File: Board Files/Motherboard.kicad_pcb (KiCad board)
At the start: 2 copper layers, 106.1 x 155 mm, 77 parts, among them P1 72-Pin Connector, P2 PowerSw, P3 ResetSw, P4 Controller_Port, P6 RF-Mod, Q1 2SA937, Q2 2SC2021, T1 08RB01, U1 6116 (WRAM), U2 74HC373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

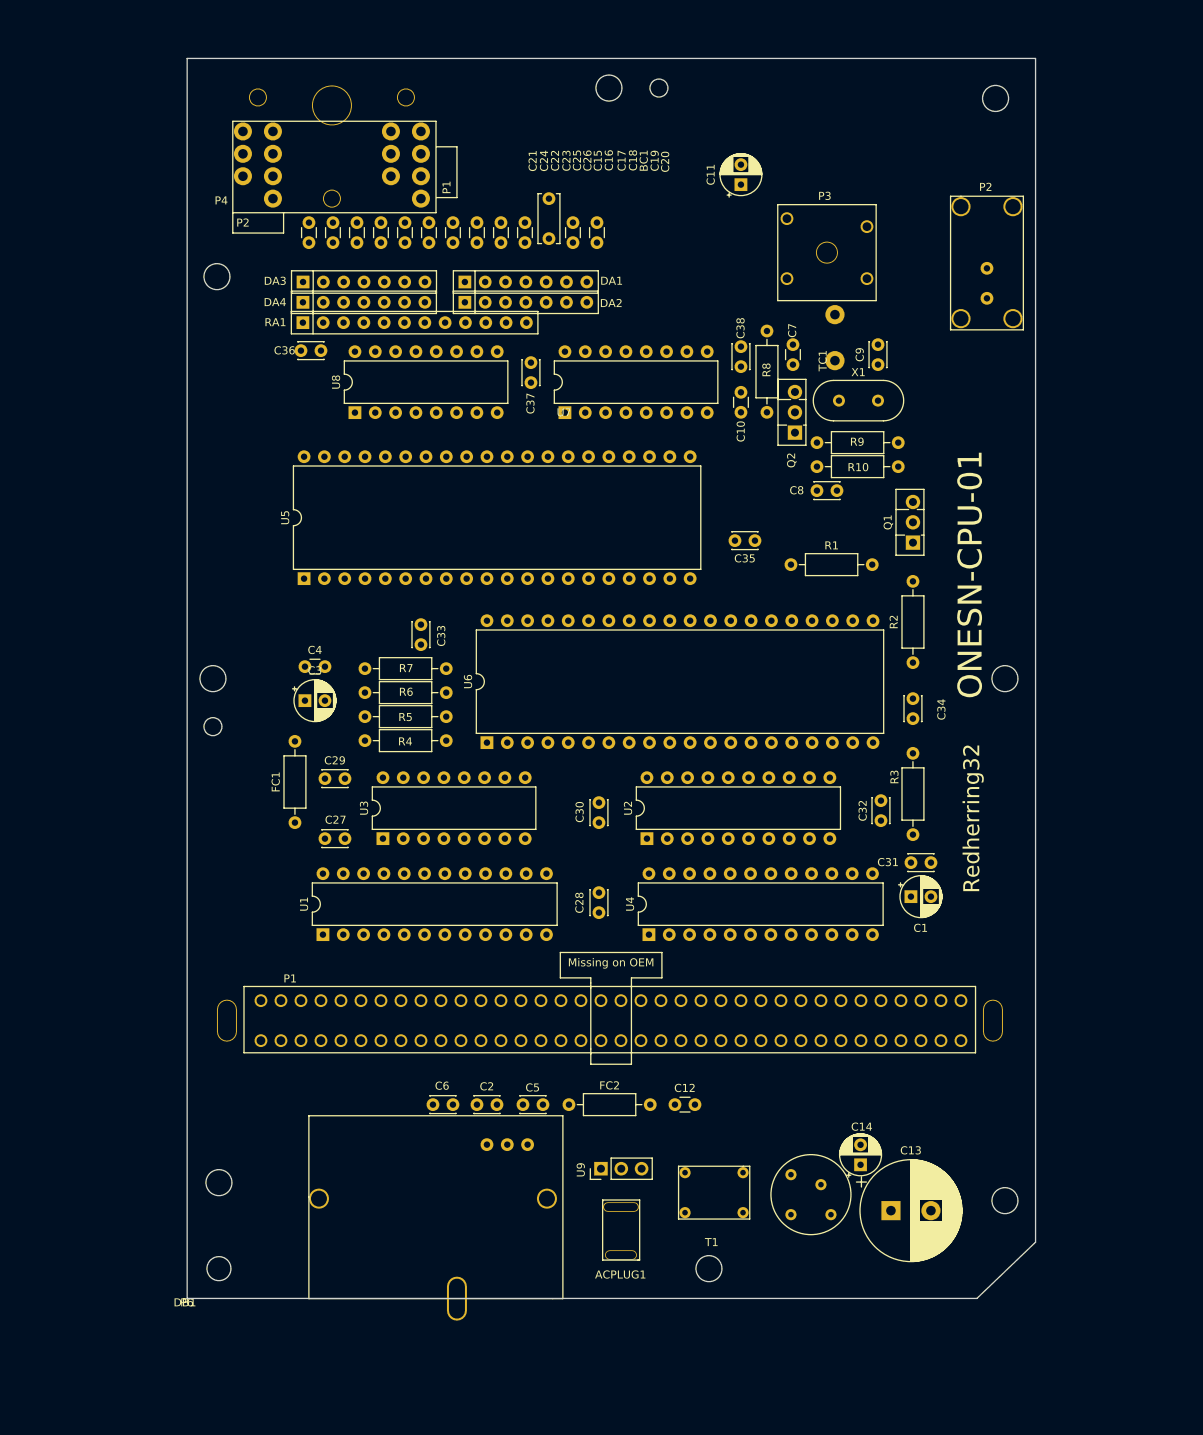
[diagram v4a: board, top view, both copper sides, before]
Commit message: Almost done
+ Added zone cutouts to make copper pours more like OEM shape
+ Edited schematic to be more readable

TO-DO:
* Finish cutouts
* Verify mounting, alignment, and connector hole placement and sizing.
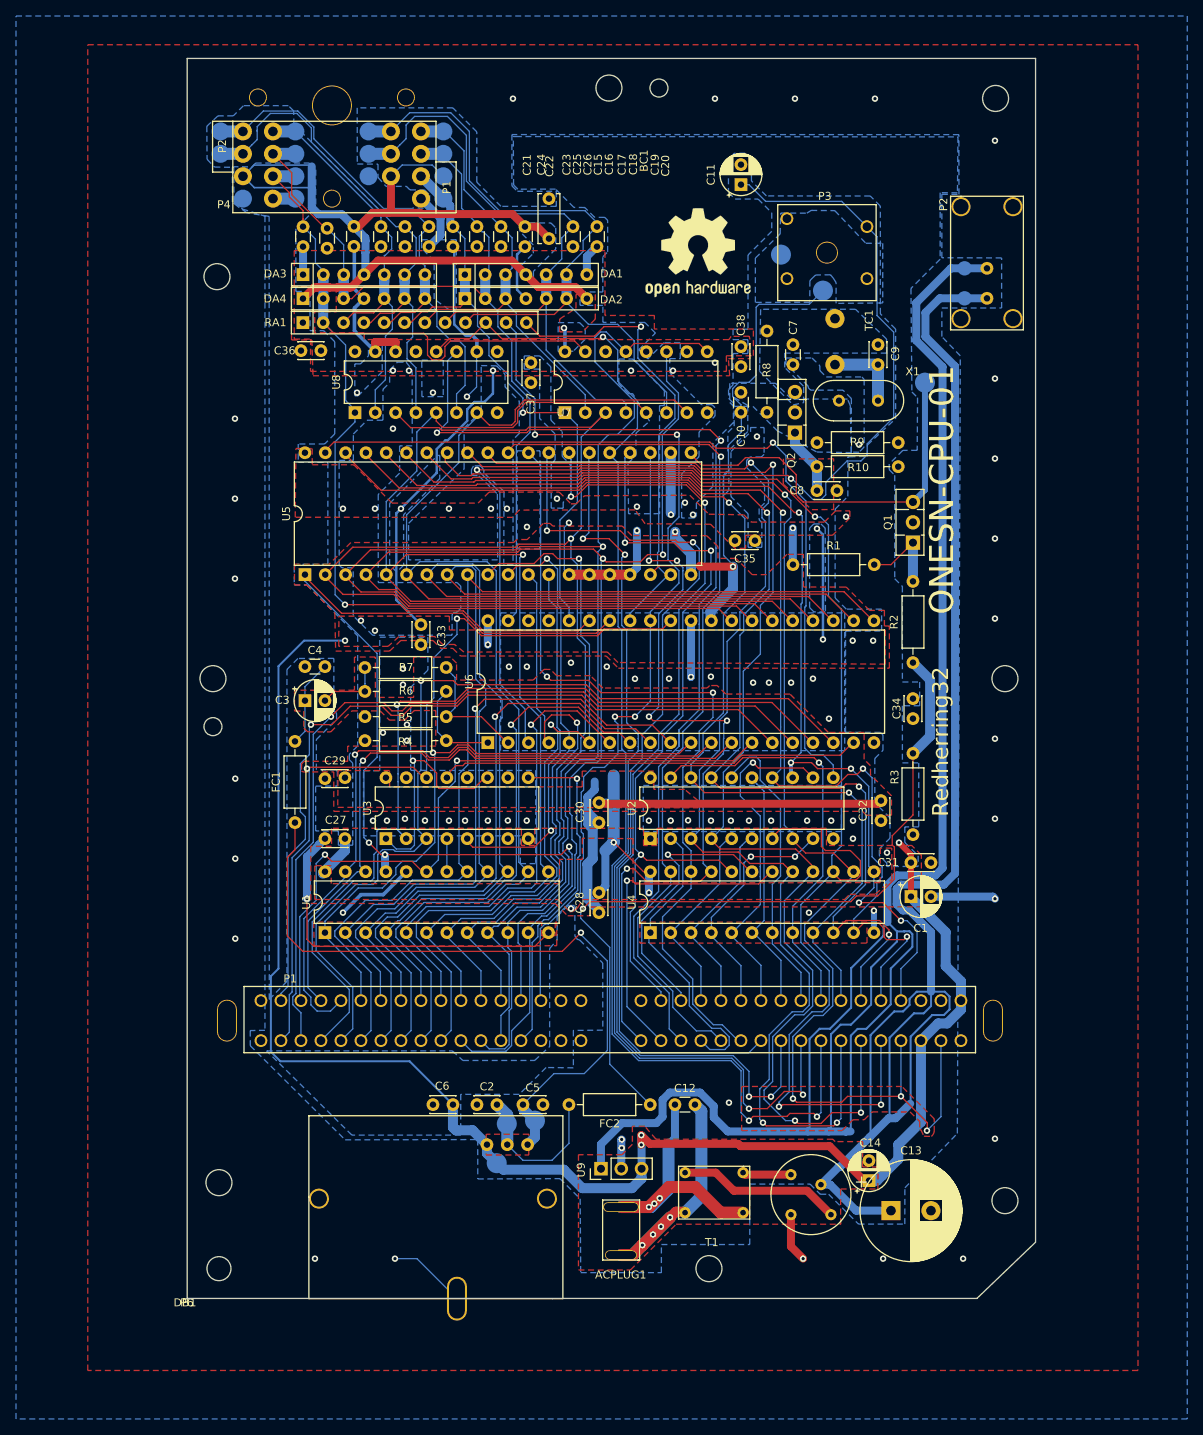
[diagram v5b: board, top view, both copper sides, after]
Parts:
- added  : TestPoint_Pad_D2.5mm, TestPoint:TestPoint_Pad_D2.5mm, B.Cu at (38.7, -16.9)
- added  : TestPoint_Pad_D2.5mm, TestPoint:TestPoint_Pad_D2.5mm, B.Cu at (40.0, -21.9)
- added  : TestPoint_Pad_D2.5mm, TestPoint:TestPoint_Pad_D2.5mm, B.Cu at (43.6, -21.9)
- added  : TestPoint_Pad_D2.5mm, TestPoint:TestPoint_Pad_D2.5mm, B.Cu at (92.2, -114.5)
- added  : TestPoint_Pad_D2.5mm, TestPoint:TestPoint_Pad_D2.5mm, B.Cu at (74.2, -130.5)
- added  : TestPoint_Pad_D2.5mm, TestPoint:TestPoint_Pad_D2.5mm, B.Cu at (79.5, -126.0)
- added REF**: OSHW-Logo2_14.6x12mm_SilkScreen, Symbol:OSHW-Logo2_14.6x12mm_SilkScreen, F.Cu at (63.9, -130.8)
- moved FC2 10.2 mm to (57.9, -24.2), turned to 180 degrees
- moved C14 2.24 mm to (85.2, -14.8)
- moved C22 1.01 mm to (17.5, -133.8)
- moved DA1 0.92 mm to (34.7, -128.0)
- moved DA3 0.92 mm to (14.5, -128.0)
- moved C21 0.89 mm to (14.5, -134.0)
- moved C24 0.60 mm to (20.9, -131.5)
- moved U5 0.51 mm to (14.8, -90.5)
- moved C15 0.50 mm to (33.2, -134.0)
- moved C16 0.50 mm to (36.2, -134.0)
- moved C17 0.50 mm to (39.2, -134.0)
- moved C18 0.50 mm to (42.2, -134.0)
- moved C19 0.50 mm to (48.2, -134.0)
- moved C20 0.50 mm to (51.2, -134.0)
- moved C23 0.50 mm to (24.2, -134.0)
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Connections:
- net /CIC-TO-CART renamed Net-(P1-Pad34)
- net /CIC-TO-MB renamed Net-(P1-Pad35)
- C11 pad 1: /RST -> /~RST
- C12 pad 1: Net-(C12-Pad1) -> Net-(ACPLUG1-Pad2)
- C12 pad 2: Net-(C12-Pad2) -> Net-(ACPLUG1-Pad1)
- C24 pad 2: Net-(C24-Pad2) -> /VCC
- C7 pad 1: Net-(C7-Pad1) -> /GND
- C7 pad 2: /GND -> Net-(C7-Pad2)
- C9 pad 2: Net-(C7-Pad1) -> Net-(C7-Pad2)
- DB1 pad 3: Net-(C12-Pad1) -> Net-(DB1-Pad3)
- DB1 pad 4: Net-(C12-Pad2) -> Net-(DB1-Pad4)
- FC2 pad 1: /VIDEO -> Net-(FC2-Pad1)
- FC2 pad 2: Net-(FC2-Pad2) -> /VIDEO
- P1 pad 70: /CIC-RST -> /VCC
- P3 pad 1: /RST -> /~RST
- P4 pad 3: (no net) -> /GND
- P4 pad 4: (no net) -> /GND
- P4 pad 5: (no net) -> /GND
- P4 pad 6: (no net) -> /GND
- Q2 pad 3: Net-(C7-Pad1) -> Net-(C7-Pad2)
- R2 pad 1: Net-(FC2-Pad2) -> Net-(FC2-Pad1)
- R3 pad 2: Net-(FC2-Pad2) -> Net-(FC2-Pad1)
- R6 pad 1: /SOUND-1 -> Net-(C3-Pad2)
- R6 pad 2: Net-(C3-Pad2) -> /SOUND-1
- R7 pad 1: /SOUND-2 -> Net-(C3-Pad2)
- R7 pad 2: Net-(C3-Pad2) -> /SOUND-2
- R8 pad 2: Net-(C7-Pad1) -> Net-(C7-Pad2)
- R9 pad 1: /VCC -> Net-(C10-Pad2)
- R9 pad 2: Net-(C10-Pad2) -> /VCC
- T1 pad 2: Net-(C12-Pad1) -> Net-(DB1-Pad4)
- T1 pad 4: Net-(C12-Pad2) -> Net-(DB1-Pad3)
- TC1 pad 1: Net-(C7-Pad1) -> Net-(C9-Pad1)
- TC1 pad 2: Net-(C9-Pad1) -> Net-(C7-Pad2)
- U7 pad 11: /CPU-D4 -> /CPU-D2
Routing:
- net /VCC: track 0.00 -> 465.4 mm, vias 0 -> 36
- net Net-(P2-Pad2): track 0.00 -> 228.9 mm
- net /GND: track 0.00 -> 215.8 mm, vias 0 -> 78
- net /CPU-D1: track 0.00 -> 209.3 mm, vias 0 -> 1
- net /CPU-D0: track 0.00 -> 204.6 mm, vias 0 -> 1
- net /CPU-D3: track 0.00 -> 202.6 mm, vias 0 -> 1
- net /CPU-D4: track 0.00 -> 194.6 mm
- net /CPU-D2: track 0.00 -> 194.5 mm, vias 0 -> 2
- net Net-(C13-Pad1): track 0.00 -> 189.6 mm
- net /PPU-D4: track 0.00 -> 174.7 mm, vias 0 -> 4
- net /PPU-D5: track 0.00 -> 174.5 mm, vias 0 -> 3
- net /PPU-D6: track 0.00 -> 162.0 mm, vias 0 -> 3
- net /PPU-A13: track 0.00 -> 159.3 mm, vias 0 -> 3
- net /PPU-D7: track 0.00 -> 157.7 mm, vias 0 -> 3
- net /PPU-D1: track 0.00 -> 149.1 mm, vias 0 -> 3
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- added copper zone on B.Cu, net /GND
- added copper zone on F.Cu, net /GND
- added copper zone on B.Cu, net /SYS-CLK
- added copper zone on B.Cu, net /VCC
- added copper zone on F.Cu, net /VCC
- added copper zone on B.Cu, net Net-(C10-Pad2)
- added copper zone on B.Cu, net Net-(C7-Pad2)
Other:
- net class Default: trace_width 0.25 -> 0.155
- net class Thin added: clearance 0.15, trace_width 0.15, via_dia 0.8, via_drill 0.4
- rule solder_mask_min_width: 0.25 -> 0.155
- rule trace_min: 0.2 -> 0.127

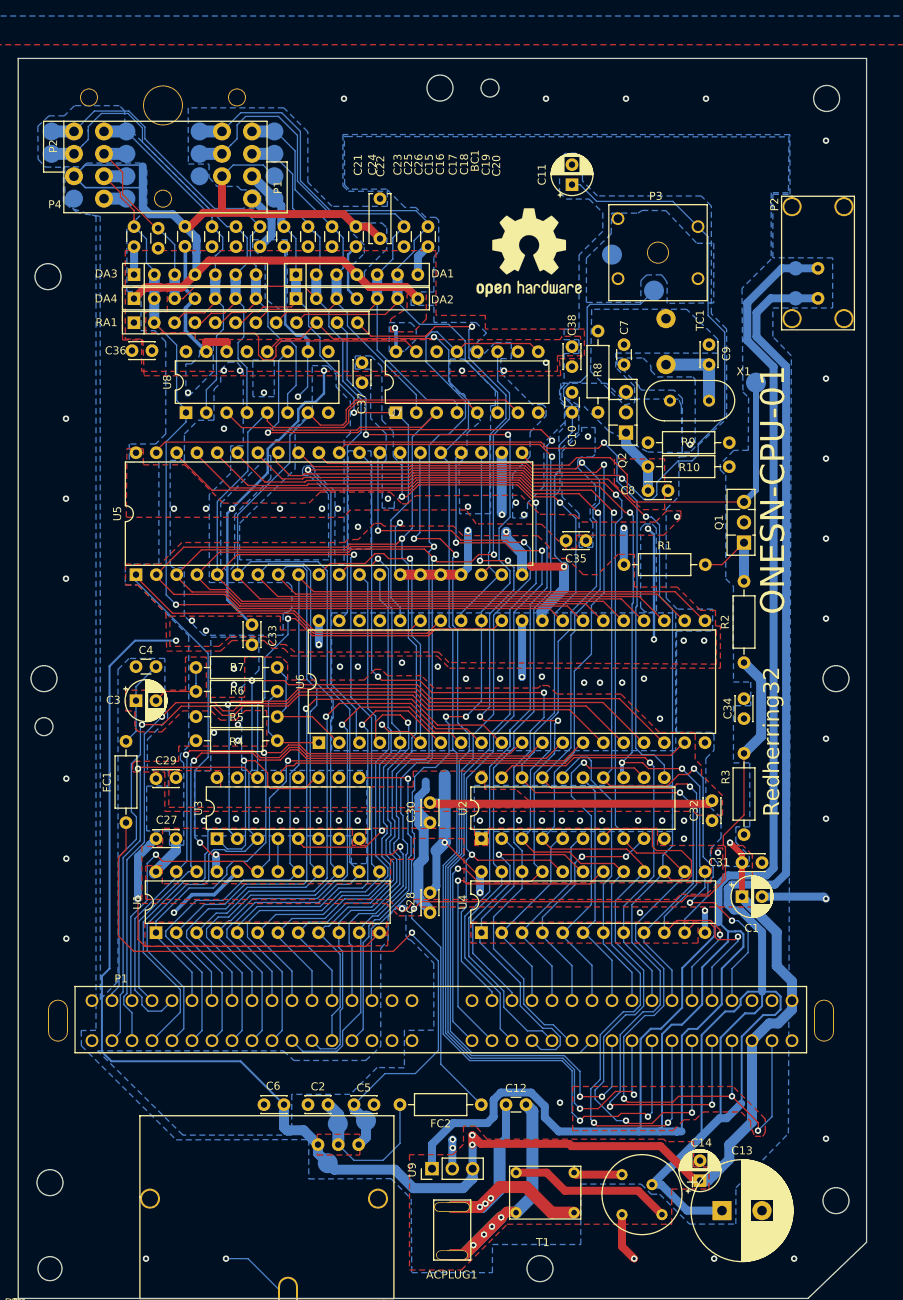
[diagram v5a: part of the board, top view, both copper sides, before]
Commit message: + Fixed hole sizing and placement issues + Updated Cartridge connector, Controller Port, PowerSwitch, and ResetSwitch footprints to fix pad placement issues + Fixed overlapping reference labeling in schematic
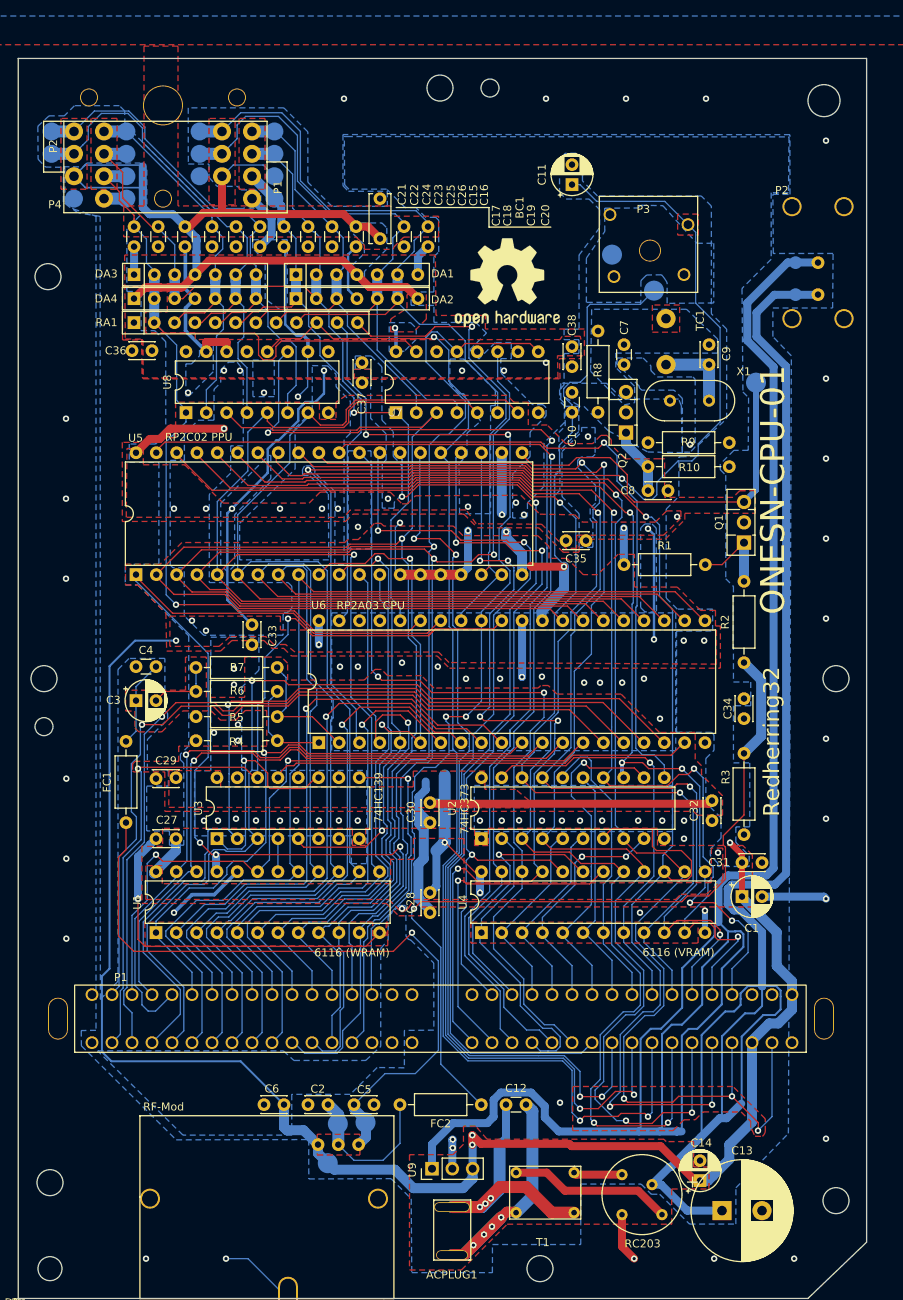
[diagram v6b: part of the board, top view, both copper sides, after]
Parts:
- P2: footprint Toploader:PowerSwitch -> Toploader:PowerSwitchV2
- P3: footprint Toploader:ResetSwitch -> Toploader:ResetSwitchV2
- moved P3 11.1 mm to (83.7, -134.3)
- moved REF** 4.63 mm to (61.2, -127.0)
- moved C24 2.47 mm to (20.9, -134.0), turned to 270 degrees
- moved P1 0.25 mm to (9.25, -32.0)
- moved   0.23 mm to (43.5, -21.7)
- moved C22 0.20 mm to (17.5, -134.0)
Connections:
- C24 pad 1: /GND -> /VCC
- C24 pad 2: /VCC -> /GND
- P4 pad 6: /GND -> (no net)
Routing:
- net /VCC: track 465.4 -> 477.6 mm
- net Net-(C13-Pad1): track 189.6 -> 191.2 mm
- net /~RST: track 139.7 -> 138.7 mm
- net /CPU-A10: track 86.2 -> 85.4 mm
- net /CPU-A9: track 83.2 -> 82.5 mm
- net /CPU-A0: track 76.0 -> 75.2 mm
- net /VRAM-A10: track 34.0 -> 33.2 mm
- net /PPU-~RD: track 97.3 -> 96.5 mm
- net /PPU-D3: track 131.9 -> 131.1 mm
- net /PPU-D2: track 141.7 -> 141.0 mm
- net /PPU-D1: track 149.1 -> 148.3 mm
- net /PPU-D0: track 140.9 -> 140.2 mm
- net /PPU-A6: track 25.0 -> 24.2 mm
- net /PPU-A5: track 24.8 -> 24.0 mm
- net /PPU-A4: track 30.4 -> 29.6 mm
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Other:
- outline, holes or cut-outs redrawn
- rule pad_to_mask_clearance: 0.051 -> 0

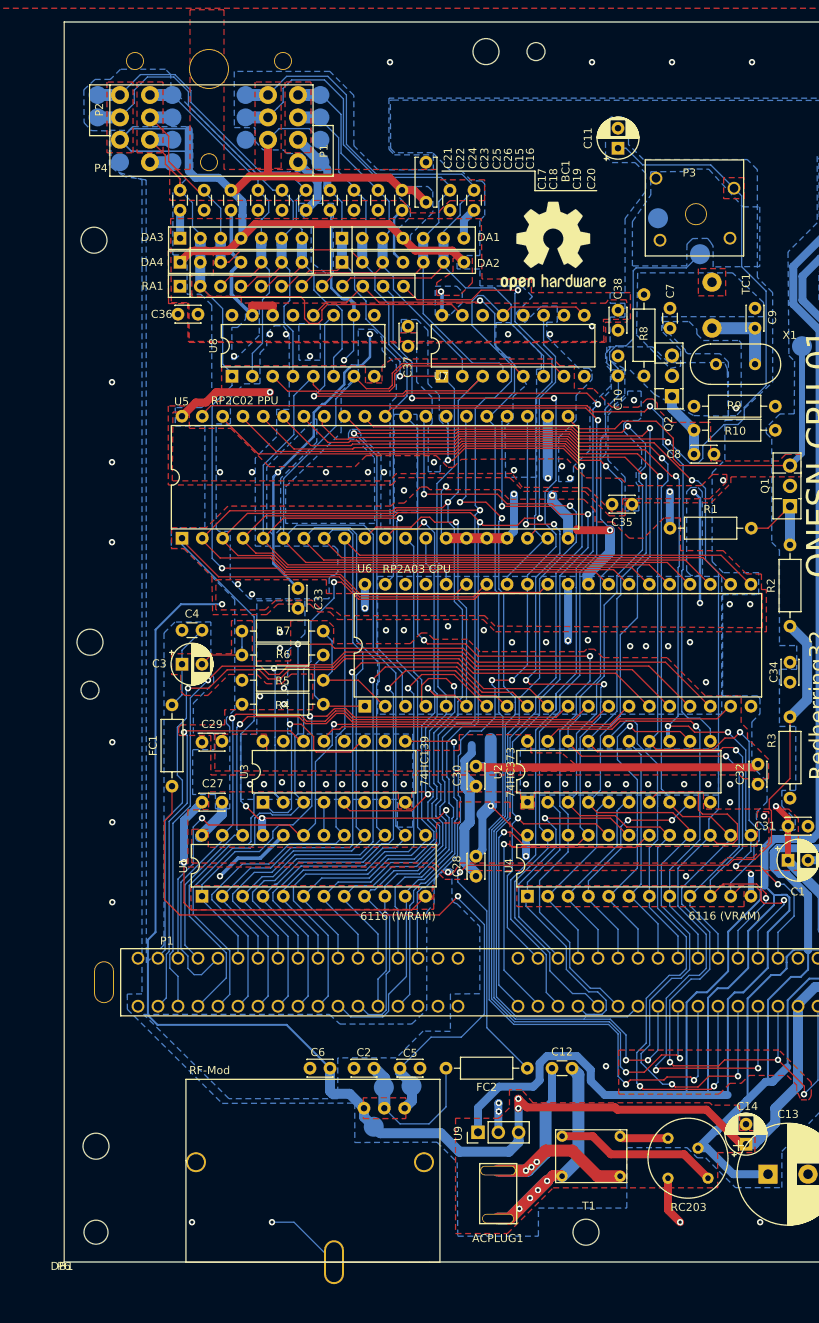
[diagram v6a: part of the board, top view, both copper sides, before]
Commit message: + Implemented fixes for issues found in testing
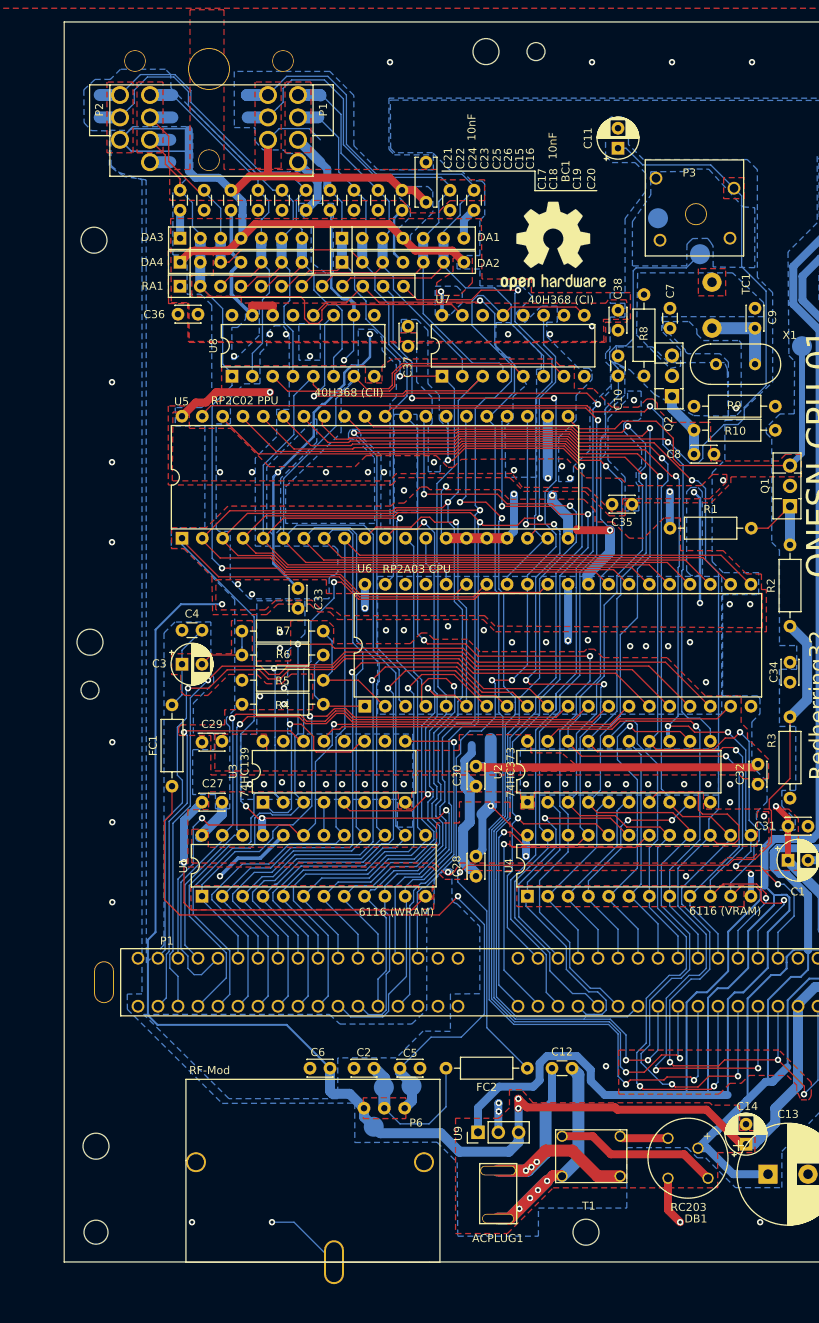
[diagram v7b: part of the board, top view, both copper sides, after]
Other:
- board text added: "+"
